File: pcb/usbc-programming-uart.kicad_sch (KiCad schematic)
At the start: 27 parts, among them J3 HC-TYPE-C-16P-01A, Q3 MMBT2222A, Q4 MMBT2222A, SW1 RST, SW2 BOOT, U11 CH334R, U12 LM1117IMPX-3.3, U13 CH340C, Y1 12MHz

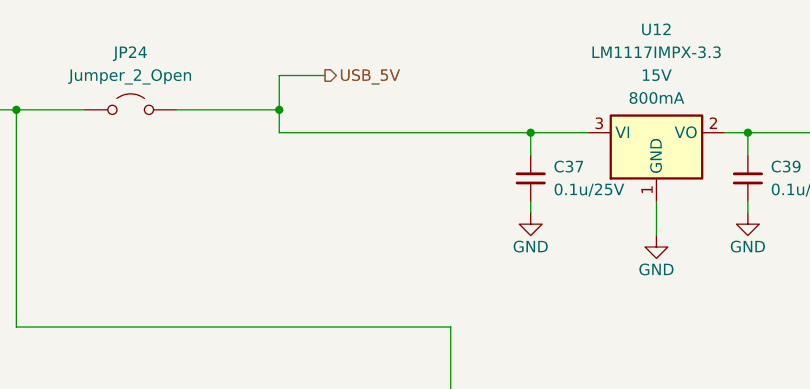
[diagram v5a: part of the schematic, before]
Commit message: Fix DRC/ERC issues: PWR_FLAG on USB-C UART VBUS net, BAS116 NC pin resync
- Add PWR_FLAG to the unpowered net on usbc-programming-uart.kicad_sch
  to resolve an ERC power-pin-not-driven error
- Re-sync D2/D3 (BAS116LT1G) in peripherals.kicad_sch from the library
  to pick up the corrected pin 2 electrical type

Co-Authored-By: Claude Sonnet 5 <noreply@anthropic.com>
Claude-Session: https://claude.ai/code/session_01LhLkuH6sQ5GbUZ61bG7p2h
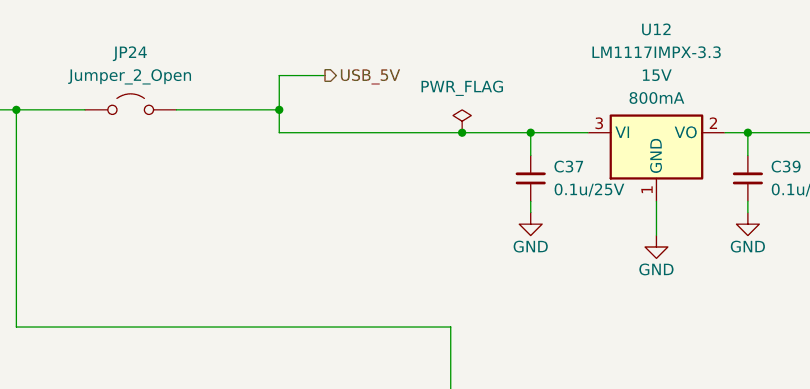
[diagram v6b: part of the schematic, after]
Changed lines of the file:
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@@
 	)
 	(junction
+		(at 215.9 25.4)
+		(diameter 0)
+		(color 0 0 0 0)
+	)
+	(junction
 		(at 100.33 180.34)
 		(diameter 0)
@@
 	(wire
 		(pts
-			(xy 195.58 25.4) (xy 223.52 25.4)
+			(xy 195.58 25.4) (xy 215.9 25.4)
 		)
 		(stroke
@@
 	(wire
 		(pts
+			(xy 215.9 25.4) (xy 223.52 25.4)
+		)
+		(stroke
+			(width 0)
+			(type default)
+		)
+	)
+	(wire
+		(pts
 			(xy 212.09 121.92) (xy 212.09 124.46)
 		)
@@
 					(unit 1)
 				)
+			)
+		)
+	)
+	(symbol
+		(lib_id "power:PWR_FLAG")
+		(at 215.9 25.4 0)
+		(unit 1)
+		(body_style 1)
+		(exclude_from_sim no)
+		(in_bom yes)
+		(on_board yes)
+		(in_pos_files yes)
+		(dnp no)
+		(fields_autoplaced yes)
+		(property "Reference" "#FLG021"
+			(at 215.9 23.495 0)
+			(hide yes)
+			(show_name no)
+			(do_not_autoplace no)
+			(effects
+				(font
+					(size 1.27 1.27)
+				)
+			)
+		)
+		(property "Value" "PWR_FLAG"
+			(at 215.9 20.32 0)
+			(show_name no)
+			(do_not_autoplace no)
+			(effects
+				(font
+					(size 1.27 1.27)
+				)
+			)
+		)
+		(property "Footprint" ""
+			(at 215.9 25.4 0)
+			(hide yes)
+			(show_name no)
+			(do_not_autoplace no)
+			(effects
+				(font
+					(size 1.27 1.27)
+				)
+			)
+		)
+		(property "Datasheet" ""
+			(at 215.9 25.4 0)
+			(hide yes)
+			(show_name no)
+			(do_not_autoplace no)
+			(effects
+				(font
+					(size 1.27 1.27)
+				)
+			)
+		)
+		(property "Description" "Special symbol for telling ERC where power comes from"
+			(at 215.9 25.4 0)
+			(hide yes)
+			(show_name no)
+			(do_not_autoplace no)
+			(effects
+				(font
+					(size 1.27 1.27)
+				)
+			)
+		)
+		(pin "1"
+		)
+		(instances
+			(project "foxhunt1"
+				(path "/8399ba4b-9428-480d-8b65-76cf154b97a5/97991d87-aeba-471b-8b55-fc9d012290ca"
+					(reference "#FLG021")
+					(unit 1)
+				)

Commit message: Wire SD card interface, fix R29/Q6/Q7 sourcing, localize datasheets project-wide
- SD card (Card1, Molex 472192001) wired to the FSPI (SPI2) peripheral:
  IO10/FSPICS0->CS, IO11/FSPID->MOSI, IO12/FSPICLK->SCLK, IO13/FSPIQ->MISO;
  shield/mounting tabs renamed SHLD and grounded; local decoupling cap added
- R29 was silently a 10k YAGEO part (RC0603FR-0710KL/C98220) sitting under a
  1M designator -- corrected to the real 1M part (RC0603FR-071ML/C105578),
  matching this rail's documented VRAW soft-latch bleed design intent
- Q6, Q7 (BSS138): added missing Manf/MPN/LCSC Part# (onsemi BSS138LT1G,
  C82045)
- C32/C36: normalized Value strings; fixed C36's Datasheet, which pointed to
  a different capacitor's PDF entirely
- Localized every remaining component's Datasheet field to a project-local
  path across all 8 schematic sheets (was a live remote URL before), per
  the new datasheet-localization task; caught and rejected a wrong-language
  and a wrong-manufacturer-clone source along the way (U8, U14, U15, Y2)
- Fixed 4 datasheet fields (Q1, D1, U6, U7) that had reverted from their
  already-localized paths back to remote URLs, apparently from a native
  KiCad symbol-library resync picking up stale library-level defaults

Co-Authored-By: Claude Sonnet 5 <noreply@anthropic.com>
Claude-Session: https://claude.ai/code/session_01LhLkuH6sQ5GbUZ61bG7p2h
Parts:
- U12: footprint Package_TO_SOT_SMD:SOT-223 -> PCM_SparkFun-Semiconductor-Standard:SOT-223-3_TabPin2; PROD_ID (none) -> IC-26292
- Y1: footprint Crystal:Crystal_SMD_2520-4Pin_2.5x2.0mm -> PCM_SparkFun-Clock:Crystal_SMD_5.0x3.2mm; PROD_ID (none) -> XTAL-
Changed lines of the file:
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@@
 			)
 		)
-		(property "Description" "CAP CER 100nF 50V X7R 0603"
+		(property "Description" "Unpolarized capacitor, small symbol"
 			(at 92.71 45.72 0)
 			(hide yes)
@@
 			)
 		)
-		(property "Description" "PTC RESET FUSE 16V 500mA 0805"
+		(property "Description" "Resettable fuse, polymeric positive temperature coefficient"
 			(at 55.88 24.13 0)
 			(hide yes)
@@
 			)
 		)
-		(property "Description" "TRANS NPN 40V 600mA SOT-23"
+		(property "Description" "600mA Ic, 40V Vce, NPN Transistor, SOT-23"
 			(at 119.38 162.56 0)
 			(hide yes)
@@
 			)
 		)
-		(property "Description" "CAP CER 10uF 25V X7R 0805"
+		(property "Description" "Unpolarized capacitor, small symbol"
 			(at 97.79 45.72 0)
 			(hide yes)
@@
 			)
 		)
-		(property "Footprint" "Crystal:Crystal_SMD_2520-4Pin_2.5x2.0mm"
+		(property "Footprint" "PCM_SparkFun-Clock:Crystal_SMD_5.0x3.2mm"
 			(at 93.98 80.01 0)
 			(hide yes)
@@
 			)
 		)
+		(property "PROD_ID" "XTAL-"
+			(at 93.98 82.55 0)
+			(hide yes)
+			(show_name no)
+			(do_not_autoplace no)
+			(effects
+				(font
+					(size 1.27 1.27)
+				)
+			)
+		)
 		(pin "2"
 		)
@@
 			)
 		)
-		(property "Description" "CAP CER 100nF 50V X7R 0603"
+		(property "Description" "Unpolarized capacitor, small symbol"
 			(at 213.36 121.92 0)
 			(hide yes)
@@
 			)
 		)
-		(property "Description" "CAP CER 100nF 50V X7R 0603"
+		(property "Description" "Unpolarized capacitor, small symbol"
 			(at 247.65 40.64 0)
 			(hide yes)
@@
 			)
 		)
-		(property "Footprint" "Package_TO_SOT_SMD:SOT-223"
+		(property "Footprint" "PCM_SparkFun-Semiconductor-Standard:SOT-223-3_TabPin2"
 			(at 237.49 45.72 0)
 			(hide yes)
@@
 			)
 		)
-		(property "Datasheet" "https://www.lcsc.com/datasheet/C23984.pdf"
+		(property "Datasheet" "http://www.ti.com/lit/ds/symlink/lm1117.pdf"
 			(at 237.49 40.64 0)
 			(hide yes)
@@
 			)
 		)
-		(property "Description" "800-mA Low-Dropout Linear Regulator"
+		(property "Description" "800mA Low-Dropout Linear Regulator, 3.3V fixed output, SOT-223"
 			(at 237.49 43.18 0)
 			(hide yes)
@@
 			)
 		)
+		(property "PROD_ID" "IC-26292"
+			(at 237.49 48.26 0)
+			(hide yes)
+			(show_name no)
+			(do_not_autoplace no)
+			(effects
+				(font
+					(size 1.27 1.27)
+				)
+			)
+		)
 		(pin "2"
 		)
@@
 			)
 		)
-		(property "Description" "CAP CER 1uF 50V X7R 0805"
+		(property "Description" "Unpolarized capacitor, small symbol"
 			(at 135.89 48.26 0)
 			(hide yes)
@@
 			)
 		)
-		(property "Description" "CAP CER 1uF 50V X7R 0805"
+		(property "Description" "Unpolarized capacitor, small symbol"
 			(at 66.04 154.94 0)
 			(hide yes)
@@
 			)
 		)
-		(property "Description" "CAP CER 100nF 50V X7R 0603"
+		(property "Description" "Unpolarized capacitor, small symbol"
 			(at 124.46 189.23 0)
 			(hide yes)
@@
 			)
 		)
-		(property "Description" "SWITCH TACTILE SPST 250gf SMD"
+		(property "Description" "Push button switch, generic, two pins"
 			(at 114.3 180.34 0)
 			(hide yes)
@@
 			)
 		)
-		(property "Description" "CAP CER 100nF 50V X7R 0603"
+		(property "Description" "Unpolarized capacitor, small symbol"
 			(at 223.52 40.64 0)
 			(hide yes)
@@
 			)
 		)
-		(property "Description" "CAP CER 100nF 50V X7R 0603"
+		(property "Description" "Unpolarized capacitor, small symbol"
 			(at 260.35 40.64 0)
 			(hide yes)
@@
 			)
 		)
-		(property "Description" "4-port USB HUB controller chip"
+		(property "Description" "USB HUB controller, QSOP-16"
 			(at 119.38 62.23 0)
 			(hide yes)
@@
 			)
 		)
-		(property "Description" "TRANS NPN 40V 600mA SOT-23"
+		(property "Description" "600mA Ic, 40V Vce, NPN Transistor, SOT-23"
 			(at 119.38 137.16 0)
 			(hide yes)
@@
 			)
 		)
-		(property "Description" "CAP CER 100nF 50V X7R 0603"
+		(property "Description" "Unpolarized capacitor, small symbol"
 			(at 231.14 121.92 0)
 			(hide yes)
@@
 			)
 		)
-		(property "Description" "CAP CER 100nF 50V X7R 0603"
+		(property "Description" "Unpolarized capacitor, small symbol"
 			(at 41.91 149.86 0)
 			(hide yes)
@@
 			)
 		)
-		(property "Description" "SWITCH TACTILE SPST 250gf SMD"
+		(property "Description" "Push button switch, generic, two pins"
 			(at 52.07 140.97 0)
 			(hide yes)
